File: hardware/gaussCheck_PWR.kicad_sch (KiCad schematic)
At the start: 18 parts, among them Q1 BSS138, Q1 BSS83P, U5 AP2112K-3.3

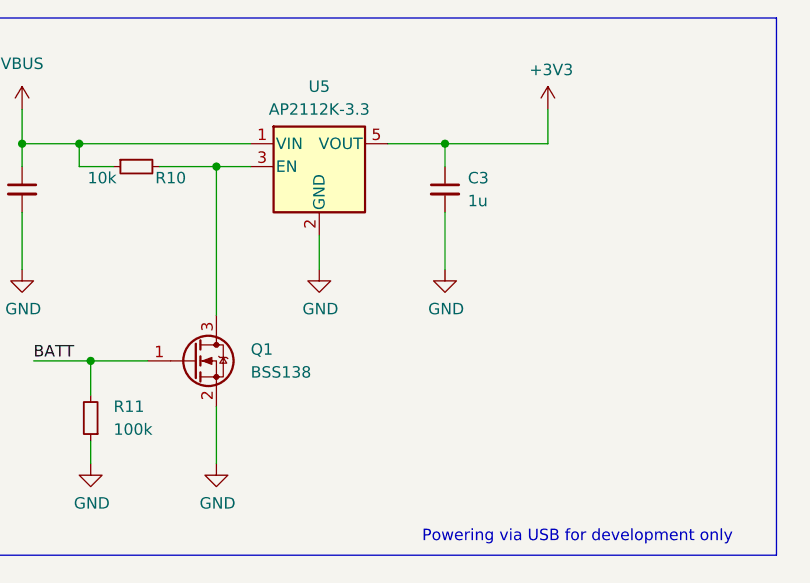
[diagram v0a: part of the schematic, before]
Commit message: added schottky diode to LDO connected en_vbat signal added a drawing of mems axis
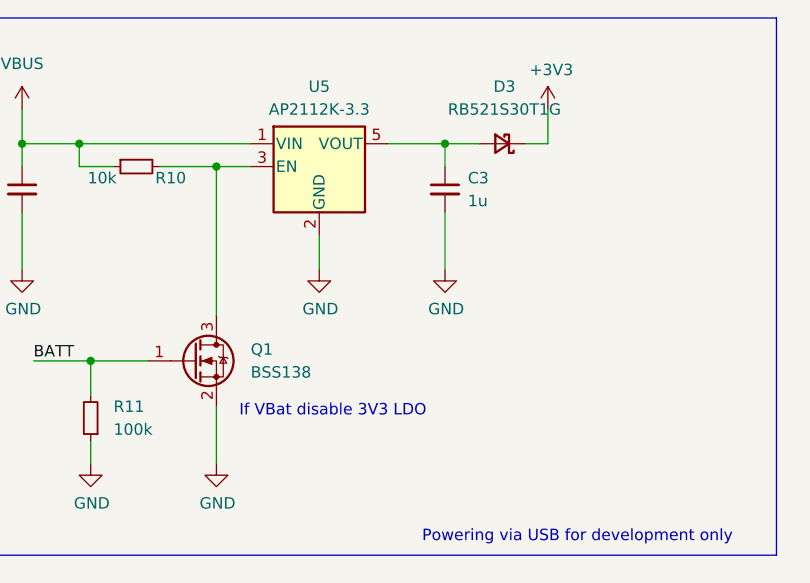
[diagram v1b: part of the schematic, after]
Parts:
- added D3: RB521S30T1G, Diode_SMD:D_SOD-523, symbol Device:D_Schottky_Small
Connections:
- net +3V3: now also D3.1 (K); no longer C3.1, U5.5 (VOUT)
- new net: C3.1, D3.2 (A), U5.5 (VOUT)
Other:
- note added: "If VBat disable 3V3 LDO"
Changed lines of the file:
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@@
     (stroke (width 0) (type default))
   )
-  (wire (pts (xy 99.06 76.2) (xy 87.63 76.2))
+  (wire (pts (xy 99.06 76.2) (xy 96.52 76.2))
     (stroke (width 0) (type default))
   )
@@
     (stroke (width 0) (type default))
   )
+  (wire (pts (xy 91.44 76.2) (xy 87.63 76.2))
+    (stroke (width 0) (type default))
+  )
   (wire (pts (xy 41.91 100.33) (xy 48.26 100.33))
     (stroke (width 0) (type default))
@@
     (stroke (width 0) (type default))
     (fill (type none))
+  )
+  (text "If VBat disable 3V3 LDO" (at 64.77 106.68 0)
+    (effects (font (size 1.27 1.27)) (justify left bottom))
   )
   (text "Powering via USB for development only\n" (at 85.09 120.65 0)
@@
         )
       )
+    )
+  )
+  (symbol (lib_id "Device:D_Schottky_Small") (at 93.98 76.2 180) (unit 1)
+    (in_bom yes) (on_board yes) (dnp no) (fields_autoplaced)
+    (property "Reference" "D3" (at 94.234 69.85 0)
+      (effects (font (size 1.27 1.27)))
+    )
+    (property "Value" "RB521S30T1G" (at 94.234 72.39 0)
+      (effects (font (size 1.27 1.27)))
+    )
+    (property "Footprint" "Diode_SMD:D_SOD-523" (at 93.98 76.2 90)
+      (effects (font (size 1.27 1.27)) hide)
+    )
+    (property "Datasheet" "https://www.onsemi.com/pdf/datasheet/rb521s30t1-d.pdf" (at 93.98 76.2 90)
+      (effects (font (size 1.27 1.27)) hide)
+    )
+    (property "Mouser" "863-RB521S30T1G" (at 93.98 76.2 0)
+      (effects (font (size 1.27 1.27)) hide)
+    )
+    (property "MPN" "RB521S30T1G" (at 93.98 76.2 0)
+      (effects (font (size 1.27 1.27)) hide)
+    )
+    (pin "1")
+    (pin "2")
+    (instances
+      (project "gaussCheck"
+        (path "/cf3c710d-e38a-496a-b88d-8d225bc2685b/c22756e4-aa1d-44a8-a547-8e3ad0f99b15"
+          (reference "D3") (unit 1)
+        )
+      )

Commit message: updated some MPNs
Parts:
- Q1: MPN (none) -> BSS138
- Q1: MPN (none) -> BSS83P
- U5: MPN (none) -> AP2112K-3.3
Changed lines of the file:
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@@
       (effects (font (size 1.27 1.27)) (justify left) hide)
+    )
+    (property "MPN" "BSS138" (at 59.69 100.33 0)
+      (effects (font (size 1.27 1.27)) hide)
     )
     (pin "3")
@@
       (effects (font (size 1.27 1.27)) hide)
     )
+    (property "MPN" "AP2112K-3.3" (at 73.66 78.74 0)
+      (effects (font (size 1.27 1.27)) hide)
+    )
     (pin "2")
     (pin "3")
@@
       (effects (font (size 1.27 1.27)) (justify left) hide)
     )
-    (pin "1")
+    (property "MPN" "BSS83P" (at 163.83 87.63 0)
+      (effects (font (size 1.27 1.27)) hide)
+    )
+    (pin "1")

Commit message: update Mouser Nr..
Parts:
- C3: MPN (none) -> C0603C105Z9VACTU; Mouser (none) -> 80-C0603C105Z9V
- C? (x2): MPN GRM188R60J106ME84D -> C1608X5R0J106K080AB; Mouser (none) -> 810-C1608X5R0J106K
- Q1: Mouser (none) -> 512-BSS138
- Q1: Mouser (none) -> 726-BSS83PH6327
- R10, R14: MPN (none) -> CRCW060310K0FKEI; Mouser (none) -> 71-CRCW060310K0FKEI
- R11, R2: MPN (none) -> CRCW0603100KFKEA; Mouser (none) -> 71-CRCW0603-100K-E3
- R4: MPN (none) -> CRCW06034K70JNEA; Mouser (none) -> 71-CRCW0603J-4.7K-E3
- U5: Mouser (none) -> 621-AP2112K-3.3TRG1
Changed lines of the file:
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@@
       (effects (font (size 1.27 1.27)) hide)
     )
+    (property "Mouser" "512-BSS138" (at 59.69 100.33 0)
+      (effects (font (size 1.27 1.27)) hide)
+    )
+    (pin "1")
+    (pin "2")
     (pin "3")
-    (pin "1")
-    (pin "2")
     (instances
       (project "gaussCheck"
@@
       (effects (font (size 1.27 1.27)) hide)
     )
-    (property "MPN" "GRM188R60J106ME84D" (at 91.44 156.21 0)
+    (property "MPN" "C1608X5R0J106K080AB" (at 91.44 156.21 0)
+      (effects (font (size 1.27 1.27)) hide)
+    )
+    (property "Mouser" "810-C1608X5R0J106K" (at 91.44 156.21 0)
       (effects (font (size 1.27 1.27)) hide)
     )
@@
       (effects (font (size 1.27 1.27)) hide)
     )
-    (pin "2")
-    (pin "1")
+    (property "MPN" "CRCW060310K0FKEI" (at 161.29 106.68 0)
+      (effects (font (size 1.27 1.27)) hide)
+    )
+    (property "Mouser" "71-CRCW060310K0FKEI" (at 161.29 106.68 0)
+      (effects (font (size 1.27 1.27)) hide)
+    )
+    (pin "1")
+    (pin "2")
     (instances
       (project "gaussCheck"
@@
     )
     (property "Datasheet" "~" (at 40.64 81.28 0)
+      (effects (font (size 1.27 1.27)) hide)
+    )
+    (property "MPN" "C0603C105Z9VACTU" (at 40.64 81.28 0)
+      (effects (font (size 1.27 1.27)) hide)
+    )
+    (property "Mouser" "80-C0603C105Z9V" (at 40.64 81.28 0)
       (effects (font (size 1.27 1.27)) hide)
     )
@@
       (effects (font (size 1.27 1.27)) hide)
     )
+    (property "MPN" "CRCW06034K70JNEA" (at 161.29 99.06 0)
+      (effects (font (size 1.27 1.27)) hide)
+    )
+    (property "Mouser" "71-CRCW0603J-4.7K-E3" (at 161.29 99.06 0)
+      (effects (font (size 1.27 1.27)) hide)
+    )
     (pin "1")
     (pin "2")
@@
       (effects (font (size 1.27 1.27)) hide)
     )
-    (pin "2")
-    (pin "1")
+    (property "MPN" "CRCW060310K0FKEI" (at 53.34 78.74 0)
+      (effects (font (size 1.27 1.27)) hide)
+    )
+    (property "Mouser" "71-CRCW060310K0FKEI" (at 53.34 78.74 0)
+      (effects (font (size 1.27 1.27)) hide)
+    )
+    (pin "1")
+    (pin "2")
     (instances
       (project "gaussCheck"
@@
       (effects (font (size 1.27 1.27)) hide)
     )
+    (property "Mouser" "621-AP2112K-3.3TRG1" (at 73.66 78.74 0)
+      (effects (font (size 1.27 1.27)) hide)
+    )
+    (pin "1")
     (pin "2")
     (pin "3")
     (pin "4")
     (pin "5")
-    (pin "1")
     (instances
       (project "gaussCheck"
@@
     )
     (property "Datasheet" "~" (at 168.91 81.28 0)
+      (effects (font (size 1.27 1.27)) hide)
+    )
+    (property "MPN" "CRCW0603100KFKEA" (at 168.91 81.28 0)
+      (effects (font (size 1.27 1.27)) hide)
+    )
+    (property "Mouser" "71-CRCW0603-100K-E3" (at 168.91 81.28 0)
       (effects (font (size 1.27 1.27)) hide)
     )
@@
     )
     (property "MPN" "BSS83P" (at 163.83 87.63 0)
+      (effects (font (size 1.27 1.27)) hide)
+    )
+    (property "Mouser" "726-BSS83PH6327" (at 163.83 87.63 0)
       (effects (font (size 1.27 1.27)) hide)
     )
@@
       (effects (font (size 1.27 1.27)) hide)
     )
-    (pin "2")
-    (pin "1")
+    (property "MPN" "CRCW0603100KFKEA" (at 48.26 106.68 0)
+      (effects (font (size 1.27 1.27)) hide)
+    )
+    (property "Mouser" "71-CRCW0603-100K-E3" (at 48.26 106.68 0)
+      (effects (font (size 1.27 1.27)) hide)
+    )
+    (pin "1")
+    (pin "2")
     (instances
       (project "gaussCheck"
@@
       (effects (font (size 1.27 1.27)) hide)
     )
-    (property "MPN" "GRM188R60J106ME84D" (at 101.6 156.21 0)
+    (property "MPN" "C1608X5R0J106K080AB" (at 101.6 156.21 0)
+      (effects (font (size 1.27 1.27)) hide)
+    )
+    (property "Mouser" "810-C1608X5R0J106K" (at 101.6 156.21 0)
       (effects (font (size 1.27 1.27)) hide)
     )
@@
       (effects (font (size 1.27 1.27)) hide)
     )
+    (property "MPN" "C0603C105Z9VACTU" (at 87.63 81.28 0)
+      (effects (font (size 1.27 1.27)) hide)
+    )
+    (property "Mouser" "80-C0603C105Z9V" (at 87.63 81.28 0)
+      (effects (font (size 1.27 1.27)) hide)
+    )
